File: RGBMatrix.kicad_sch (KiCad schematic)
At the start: 239 parts, among them Q17 PNP, Q18 PNP, Q19 PNP, Q20 PNP, Q21 PNP, Q22 PNP, Q23 PNP, Q24 PNP, Q25 PNP, Q26 PNP, Q27 PNP, Q28 PNP, Q29 PNP, Q30 PNP, Q31 PNP, Q32 PNP, U1 74LS596, U2 74LS596, U3 74LS596, U4 74LS596, U5 74LS596, U6 74LS596, U7 74154

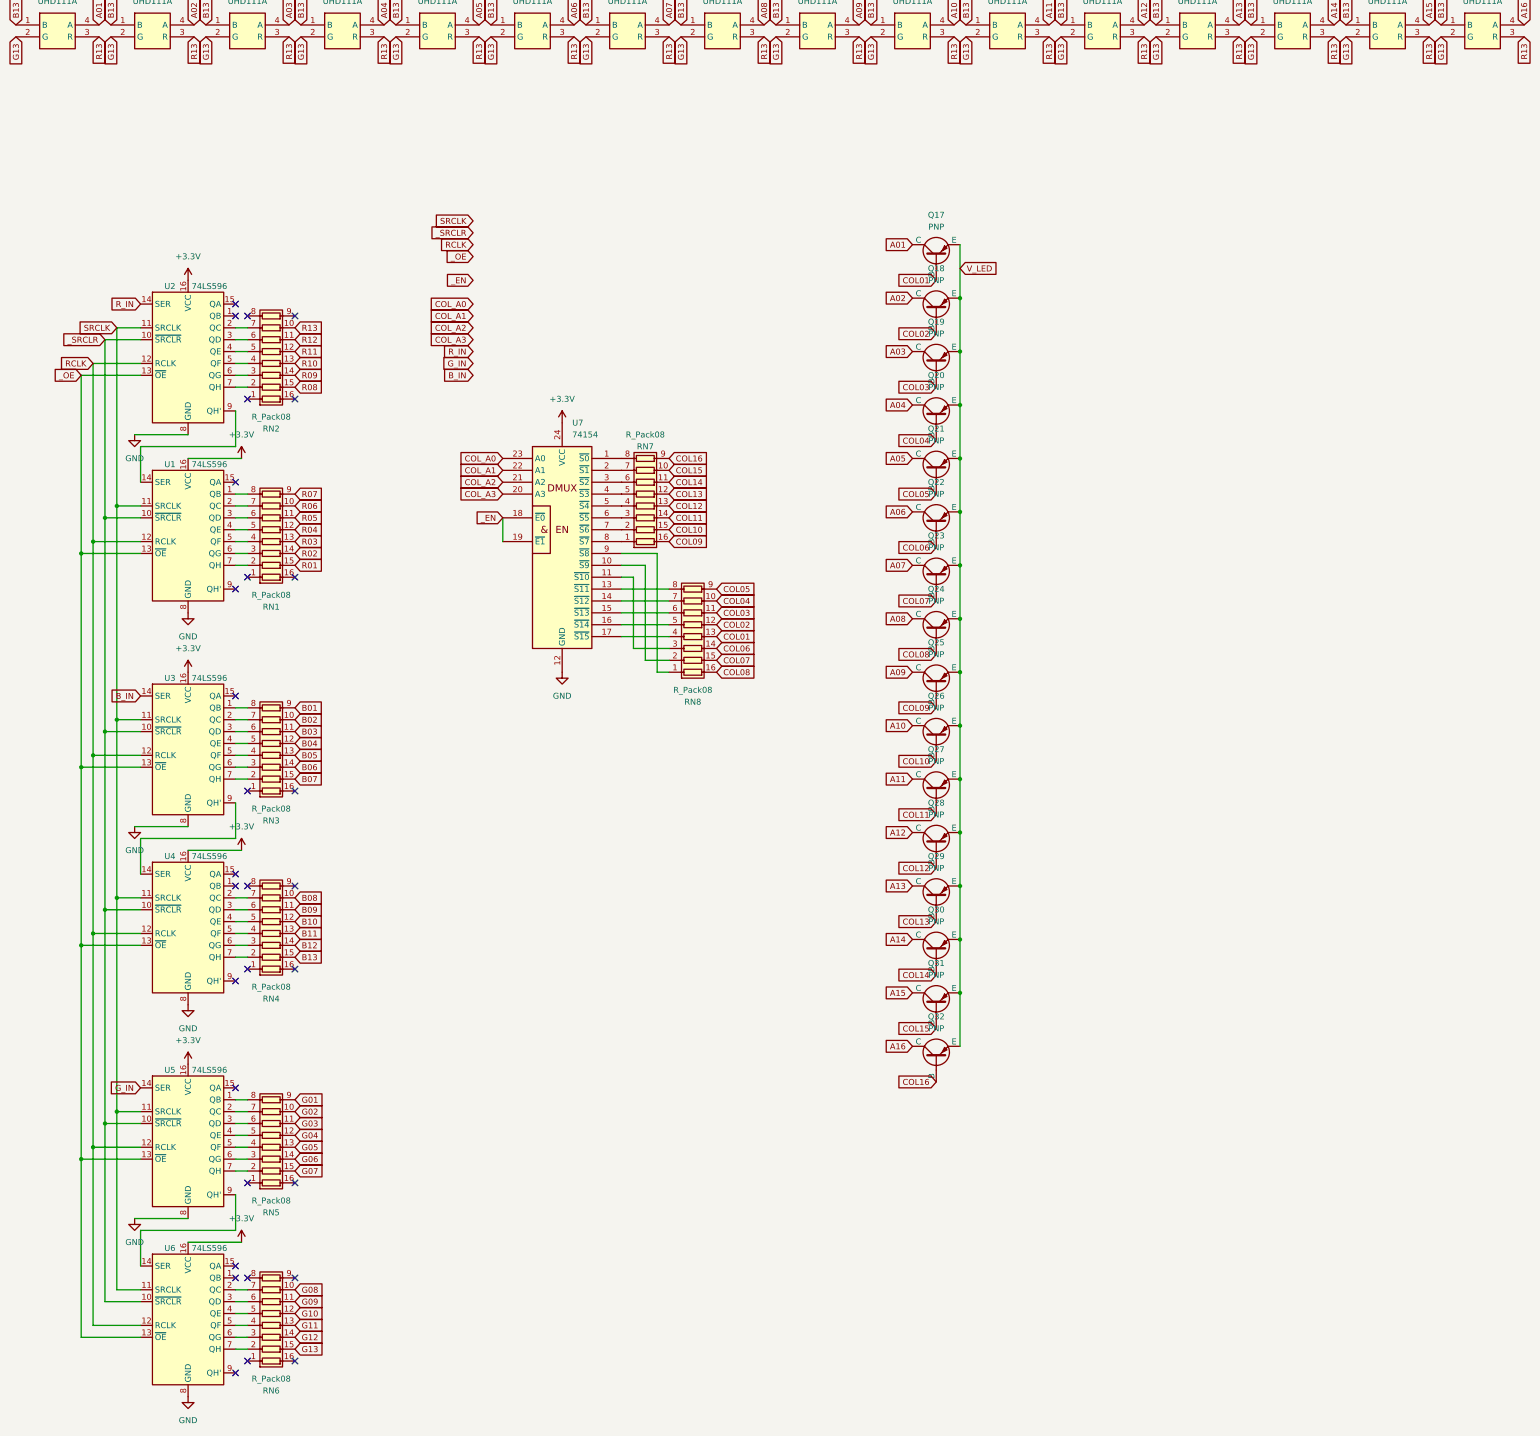
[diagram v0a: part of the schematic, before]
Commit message: progress
full wireing, ready for first check
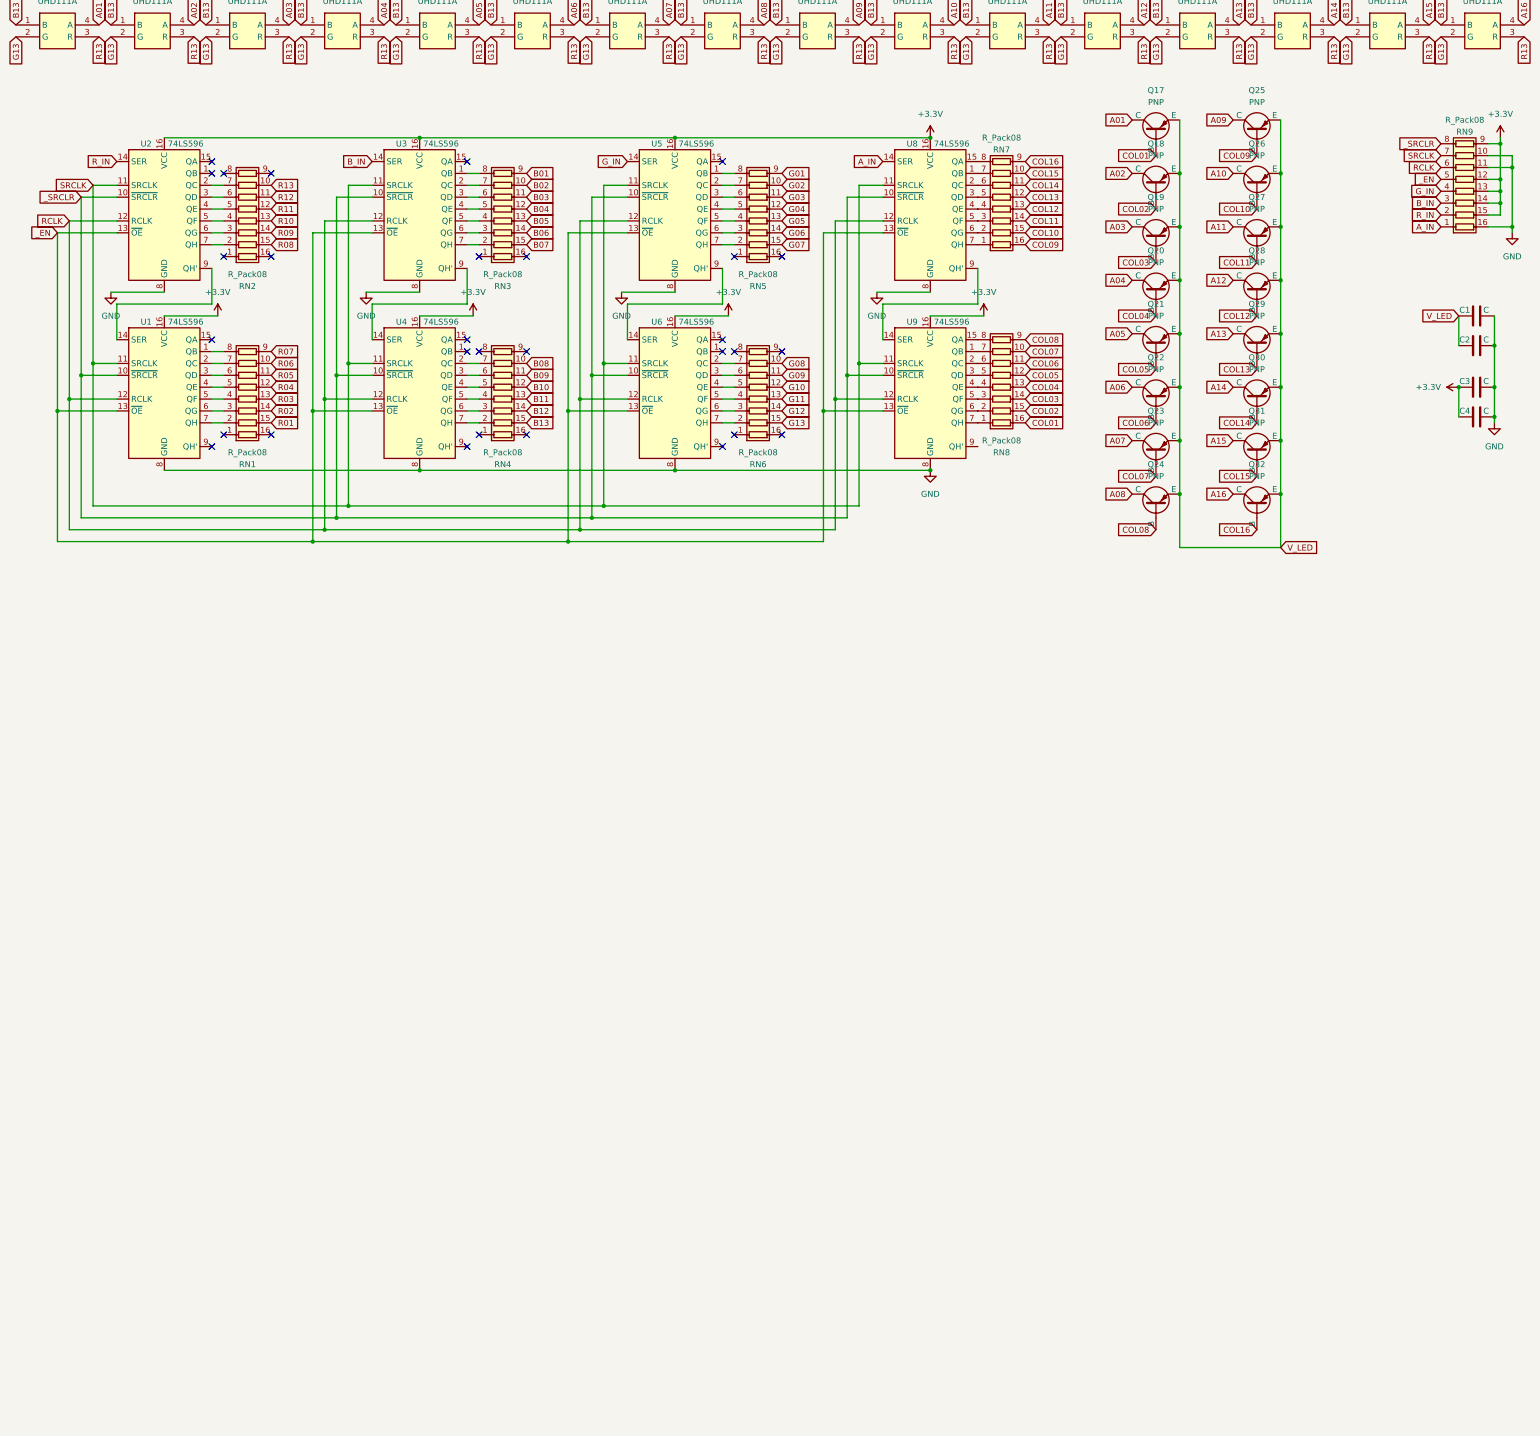
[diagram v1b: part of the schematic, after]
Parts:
- removed U7: 74154, Package_SO:TSSOP-24_4.4x7.8mm_P0.65mm, symbol 74xx_IEEE:74154
- added C1, C2, C3, C4: C, Capacitor_SMD:C_0805_2012Metric, symbol Device:C
- added RN9: R_Pack08, Resistor_SMD:R_Array_Convex_8x0602, symbol Device:R_Pack08
- added U8, U9: 74LS596, Package_SO:TSSOP-16_4.4x5mm_P0.65mm, symbol 74xx:74LS596
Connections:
- net _OE is gone; now on net _EN: U1.13 (~{OE}), U2.13 (~{OE}), U3.13 (~{OE}), U4.13 (~{OE}), U5.13 (~{OE}), U6.13 (~{OE})
- net +3.3V: now also C3.1, C4.1, RN9.12 (R5.2), RN9.13 (R4.2), RN9.14 (R3.2), RN9.15 (R2.2), RN9.9 (R8.2), U8.16 (VCC), U9.16 (VCC)
- net B_IN: now also RN9.3 (R3.1)
- net COL01: now also RN8.16 (R1.2); no longer RN8.13 (R4.2)
- net COL02: now also RN8.15 (R2.2); no longer RN8.12 (R5.2)
- net COL03: now also RN8.14 (R3.2); no longer RN8.11 (R6.2)
- net COL04: now also RN8.13 (R4.2); no longer RN8.10 (R7.2)
- net COL05: now also RN8.12 (R5.2); no longer RN8.9 (R8.2)
- net COL06: now also RN8.11 (R6.2); no longer RN8.14 (R3.2)
- net COL07: now also RN8.10 (R7.2); no longer RN8.15 (R2.2)
- net COL08: now also RN8.9 (R8.2); no longer RN8.16 (R1.2)
- net GND: now also C1.2, C2.2, C3.2, C4.2, RN9.10 (R7.2), RN9.11 (R6.2), RN9.16 (R1.2), U8.8 (GND), U9.8 (GND)
- net G_IN: now also RN9.4 (R4.1)
- net RCLK: now also RN9.6 (R6.1), U8.12 (RCLK), U9.12 (RCLK)
- net R_IN: now also RN9.2 (R2.1)
- net SRCLK: now also RN9.7 (R7.1), U8.11 (SRCLK), U9.11 (SRCLK)
- net V_LED: now also C1.1, C2.1
- net _EN: now also RN9.5 (R5.1), U8.13 (~{OE}), U9.13 (~{OE})
- net _SRCLR: now also RN9.8 (R8.1), U8.10 (~{SRCLR}), U9.10 (~{SRCLR})
- net at RN7.8 (R8.1): now also U8.15 (QA)
- net at RN8.2 (R2.1): now also U9.6 (QG)
- net at RN8.3 (R3.1): now also U9.5 (QF)
- net at RN8.8 (R8.1): now also U9.15 (QA)
- net at RN8.7 (R7.1): now also U9.1 (QB)
- net at RN8.6 (R6.1): now also U9.2 (QC)
- net at RN8.5 (R5.1): now also U9.3 (QD)
- net at RN8.4 (R4.1): now also U9.4 (QE)
- net at RN7.7 (R7.1): now also U8.1 (QB)
- net at RN7.6 (R6.1): now also U8.2 (QC)
- net at RN7.5 (R5.1): now also U8.3 (QD)
- net at RN7.4 (R4.1): now also U8.4 (QE)
- net at RN7.3 (R3.1): now also U8.5 (QF)
- net at RN7.2 (R2.1): now also U8.6 (QG)
- net at RN7.1 (R1.1): now also U8.7 (QH)
- net at RN8.1 (R1.1): now also U9.7 (QH)
- new net: U8.9 (QH'), U9.14 (SER)
- new net A_IN: RN9.1 (R1.1), U8.14 (SER)
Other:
- moved on the sheet: Q17, Q18, Q19, Q20, Q21, Q22, Q23, Q24, Q25, Q26, Q27, Q28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
